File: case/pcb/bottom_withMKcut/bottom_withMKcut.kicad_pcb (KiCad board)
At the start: 2 copper layers, 141.5 x 115.5 mm, 9 parts

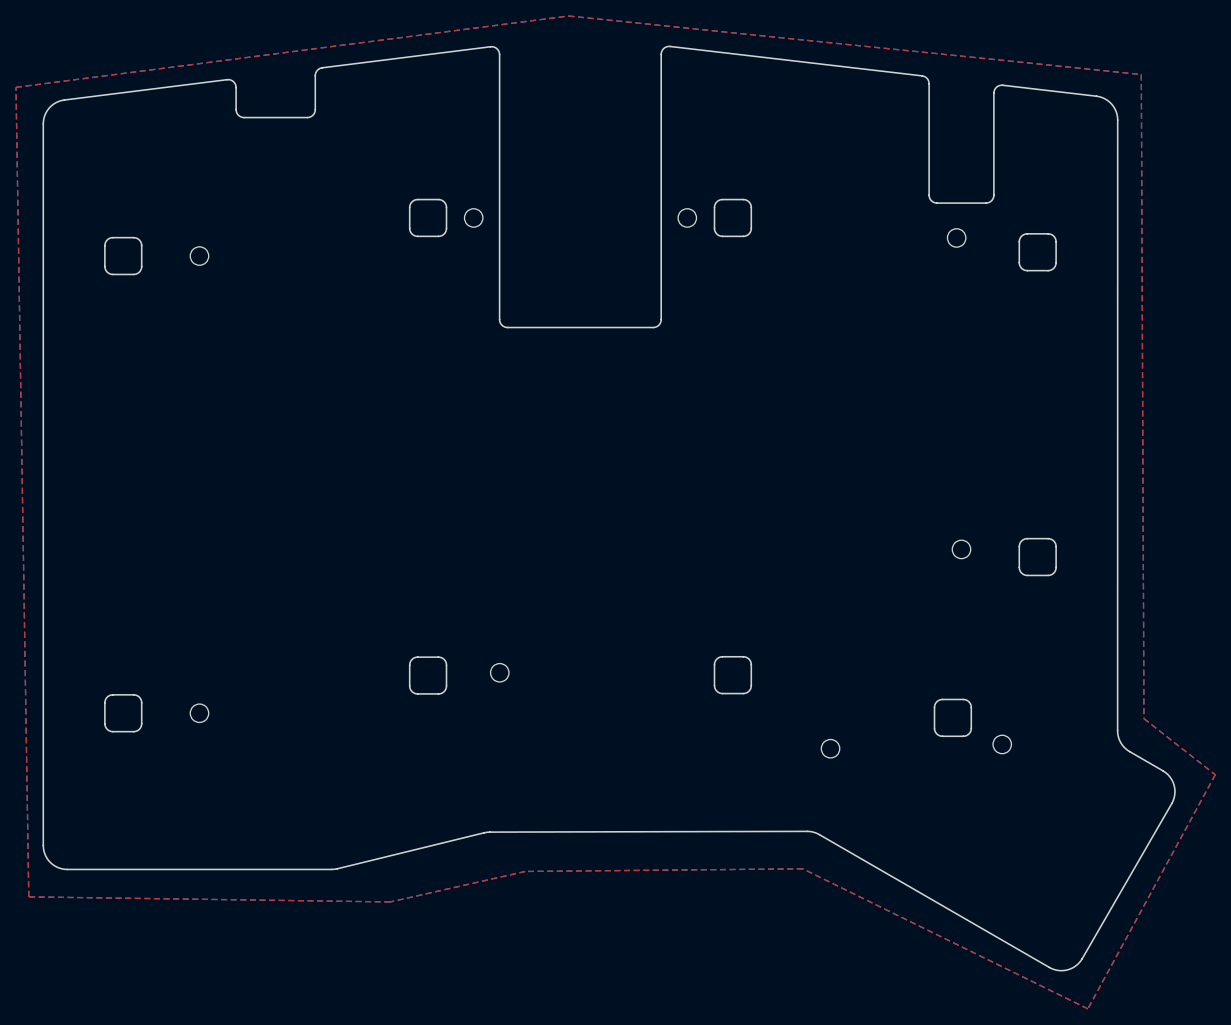
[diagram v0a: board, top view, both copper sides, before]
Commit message: add bottom pcb cases different types
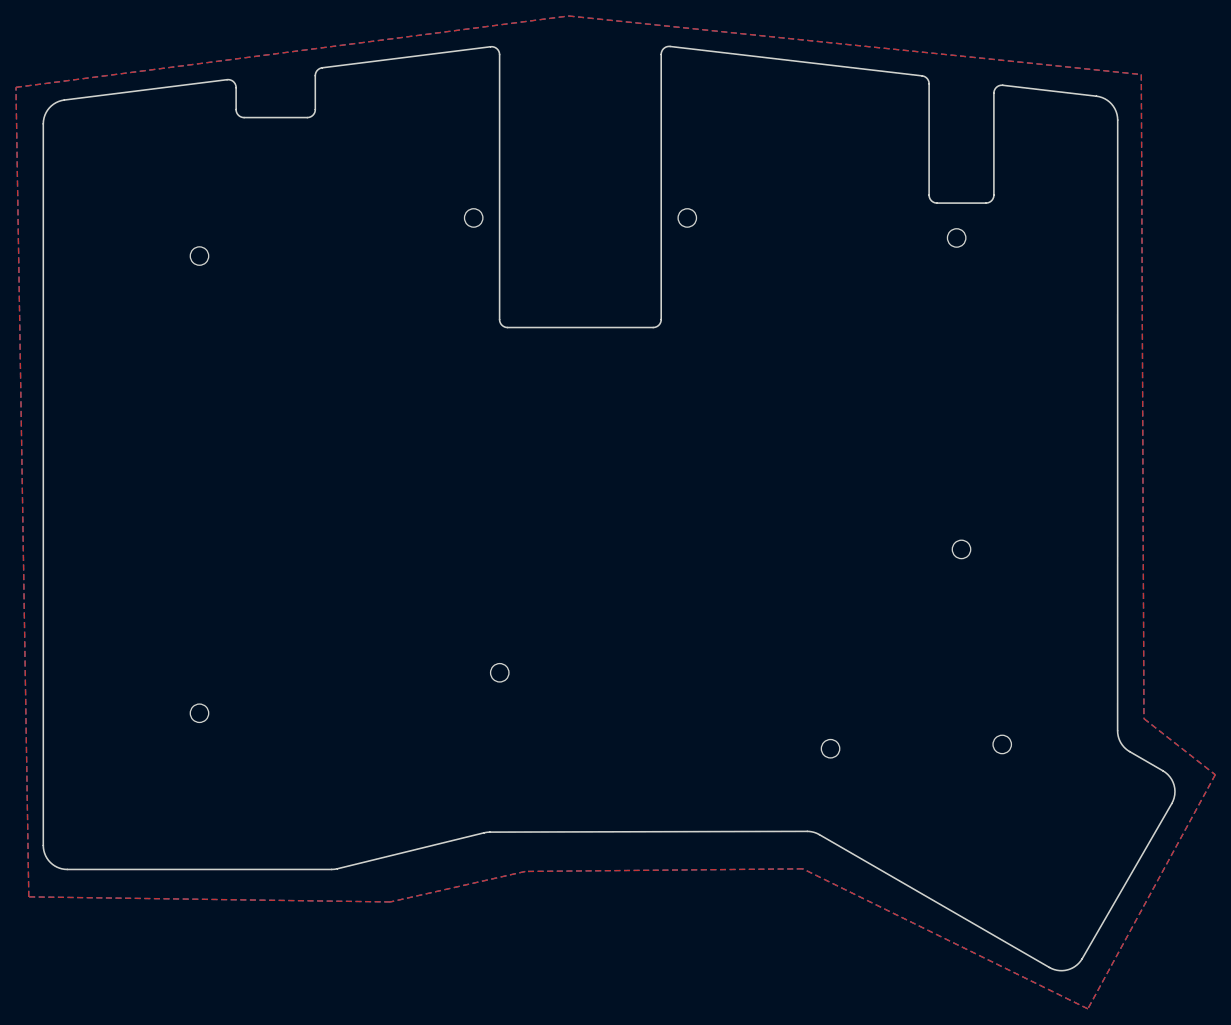
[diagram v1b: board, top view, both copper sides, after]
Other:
- outline, holes or cut-outs redrawn
